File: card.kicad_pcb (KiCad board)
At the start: 2 copper layers, 55 x 85 mm, 9 parts, among them CON1 USB-MINI-B, IC1 ATTINY44-S, P1 CONN_3X2

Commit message: rev C to fab
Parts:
- P1: moved to B.Cu
- moved D1 0.98 mm to (189.5, 88.5), turned to 270 degrees
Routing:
- net +5V: track 32.5 -> 43.7 mm, vias 1 -> 2
- net /MOSI: track 48.8 -> 59.4 mm, vias 1 -> 2
- net (no net): track 265.4 -> 257.0 mm
- net /SCK: track 37.0 -> 29.5 mm, vias 0 -> 2
- net /RST: track 30.9 -> 24.7 mm, vias 1 -> 2
- net GND: track 48.6 -> 52.4 mm, vias 3 -> 4
- net /MISO: track 32.0 -> 28.5 mm
- net N-0000017: track 11.3 -> 12.4 mm
- net N-0000016: track 13.7 -> 12.9 mm
- added copper zone on B.Cu, net (none)
- removed copper zone on F.Cu, net GND
- removed copper zone on B.Cu, net N-000001
- removed copper zone on B.Cu, net N-000002
- removed copper zone on B.Cu, net N-000003
- removed copper zone on B.Cu, net N-000005
- removed copper zone on B.Cu, net N-000006
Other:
- outline, holes or cut-outs redrawn
- board text removed: "CUTOUT"

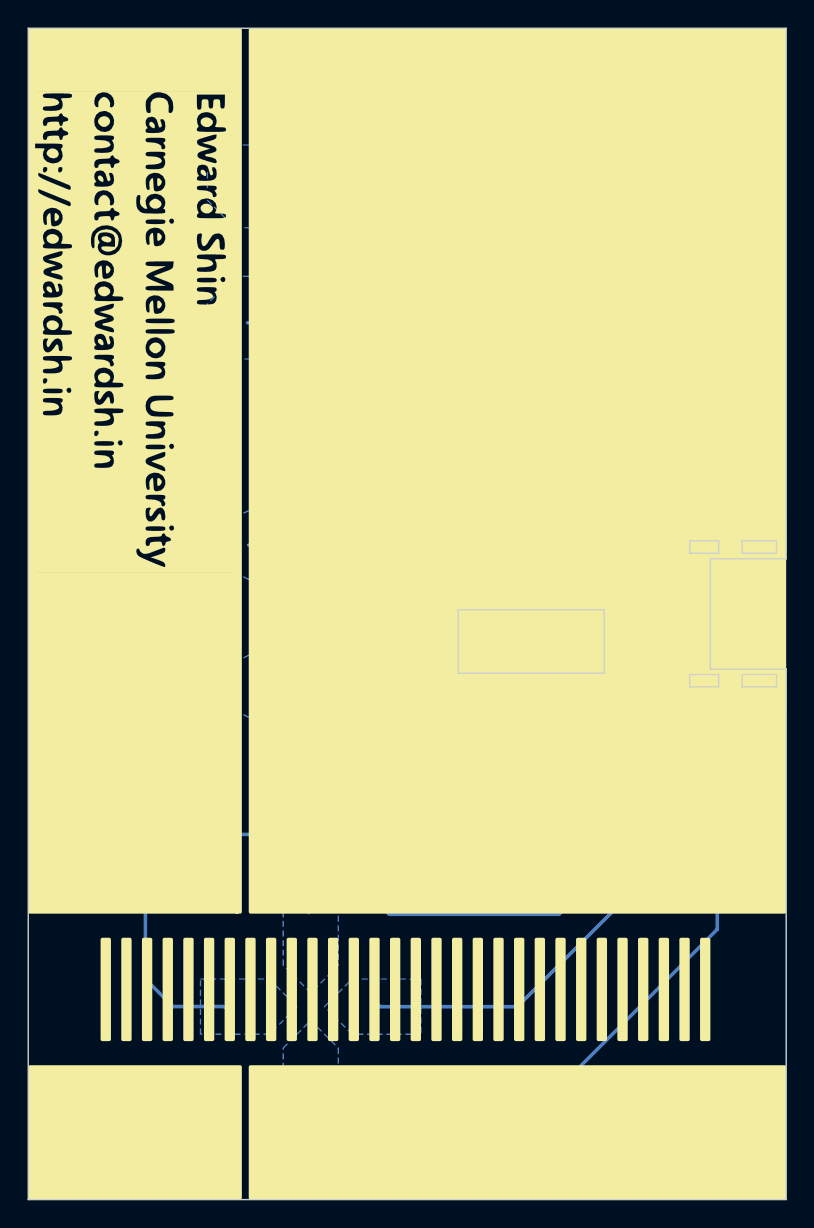
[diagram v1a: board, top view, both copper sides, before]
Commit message: working attiny26 rev sent to oshpark
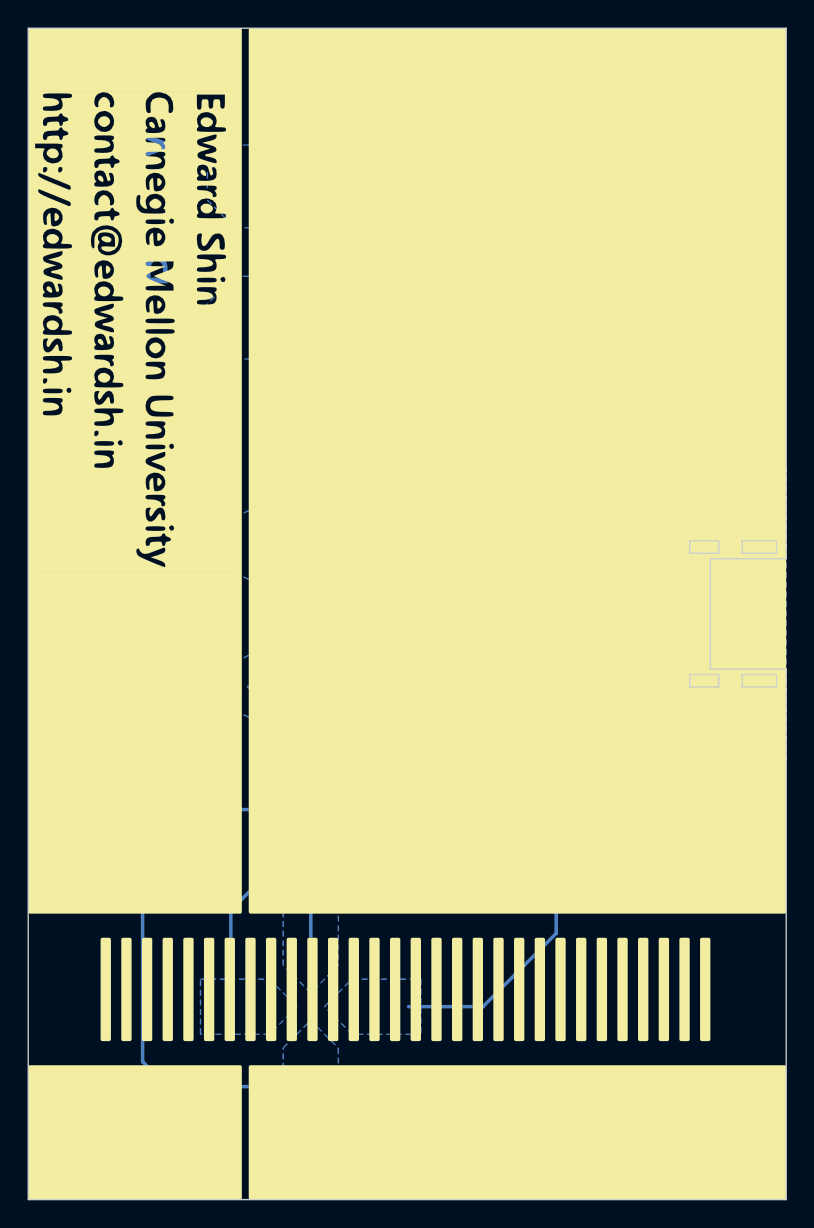
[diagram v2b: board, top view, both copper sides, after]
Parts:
- added R2: 4.7k, Resistors_SMD:R_0603_HandSoldering, B.Cu at (186.3, 85.4)
- C1: footprint SM0402_c -> Capacitors_SMD:C_0603_HandSoldering
- CON1: footprint 15542661MicroUSBB -> card:15542661MicroUSBB
- D1: footprint SMini4-F3-B -> card:SMini4-F3-B
- IC1: value ATTINY44-S -> ATTINY26-S; footprint so-14-inverted -> Housings_SOIC:SOIC-20_7.5x12.8mm_Pitch1.27mm
- P1: footprint pin_array_3x2_no_silk -> Pin_Headers:Pin_Header_Straight_2x03
- R1: footprint SM0603 -> Resistors_SMD:R_0603_HandSoldering
- RP1: footprint MNR12 -> card:MNR12
- moved P1 25.8 mm to (175.6, 80.8), turned to 270 degrees
- moved IC1 4.38 mm to (177.6, 92.5), turned to 270 degrees
- moved RP1 2.50 mm to (186.4, 89.2)
- moved C1 2.21 mm to (187.3, 97.6)
- moved R1 1.30 mm to (187.3, 93.1)
- moved D1 0.69 mm to (189.6, 89.2)
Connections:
- CON1 pad 4: (no net) -> Net-(CON1-Pad4)
- IC1 pad 1: +5V -> /MOSI
- IC1 pad 10: (no net) -> /RST
- IC1 pad 11: (no net) -> /Up
- IC1 pad 12: (no net) -> /Right
- IC1 pad 13: (no net) -> /Down
- IC1 pad 14: GND -> /Left
- IC1 pad 2: (no net) -> /MISO
- IC1 pad 3: N-000009 -> /SCK
- IC1 pad 4: /RST -> Net-(IC1-Pad4)
- IC1 pad 5: N-0000013 -> +5V
- IC1 pad 6: (no net) -> GND
- IC1 pad 7: /MOSI -> /Start
- IC1 pad 8: /MISO -> Net-(IC1-Pad8)
- IC1 pad 9: /SCK -> Net-(IC1-Pad9)
- RP1 pad 1: N-000009 -> Net-(IC1-Pad8)
- RP1 pad 2: N-0000013 -> Net-(IC1-Pad9)
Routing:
- net (no net): track 257.0 -> 0.00 mm
- net /Left: track 0.00 -> 59.4 mm
- net /MOSI: track 59.4 -> 12.0 mm, vias 2 -> 1
- net /A: track 0.00 -> 42.0 mm
- net /Down: track 0.00 -> 37.5 mm
- net /Up: track 0.00 -> 31.4 mm
- net /B: track 0.00 -> 31.2 mm
- net /Right: track 0.00 -> 29.3 mm
- net +5V: track 43.7 -> 70.1 mm, vias 2 -> 4
- net /Start: track 0.00 -> 22.3 mm, vias 0 -> 2
- net /MISO: track 28.5 -> 11.2 mm
- net /Select: track 0.00 -> 16.7 mm
- net /RST: track 24.7 -> 11.7 mm, vias 2 -> 0
- net /SCK: track 29.5 -> 16.8 mm, vias 2 -> 1
- net Net-(IC1-Pad8): track 0.00 -> 8.31 mm
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- added copper zone on B.Cu, net /A
- added copper zone on B.Cu, net /B
- added copper zone on B.Cu, net /Down
- added copper zone on B.Cu, net /Left
- added copper zone on B.Cu, net /Right
- added copper zone on B.Cu, net /Select
- added copper zone on B.Cu, net /Start
- added copper zone on B.Cu, net /Up
- removed copper zone on B.Cu, net (none)
- removed copper zone on B.Cu, net /MISO
- removed copper zone on B.Cu, net /MOSI
- removed copper zone on B.Cu, net /SCK
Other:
- outline, holes or cut-outs redrawn

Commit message: v3, updated with exposed capacitive pads
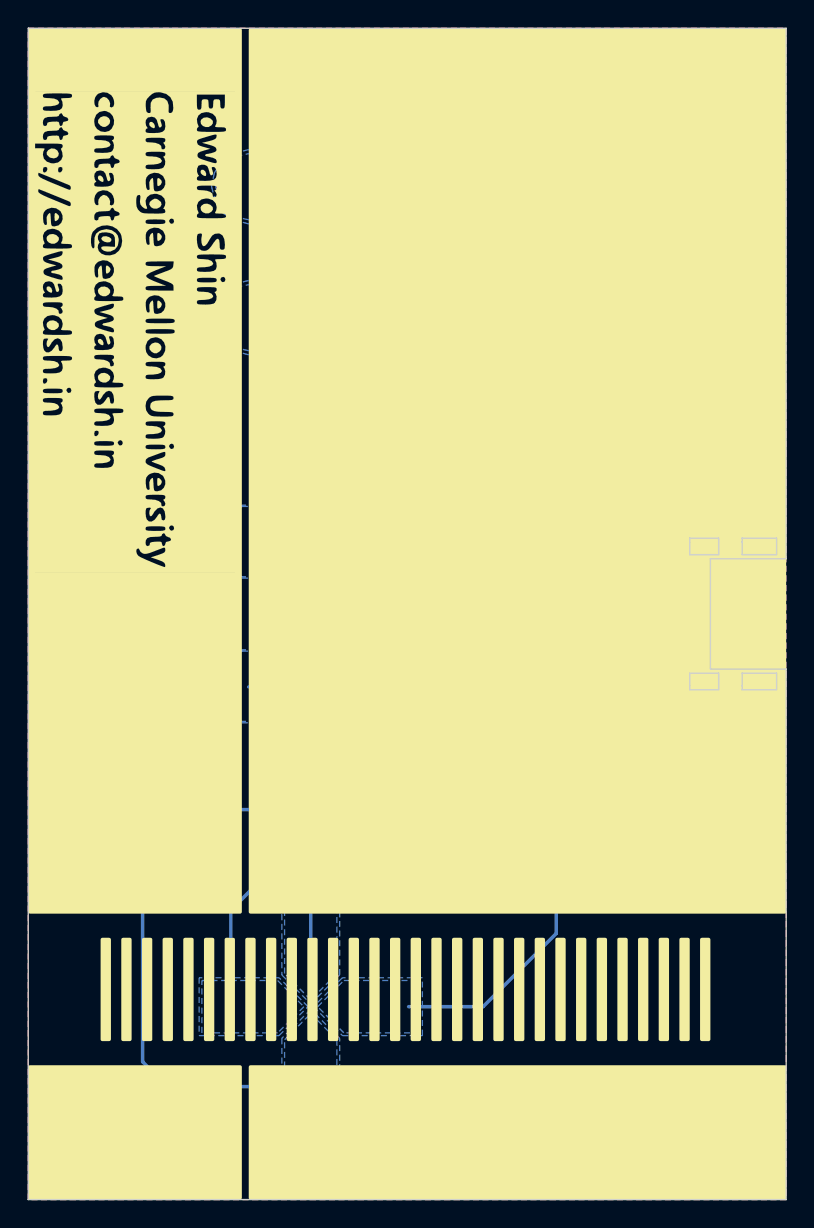
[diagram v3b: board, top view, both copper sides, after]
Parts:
- moved P1 1.90 mm to (175.6, 82.7)
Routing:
- net /SCK: track 16.8 -> 12.8 mm
- net /MISO: track 11.2 -> 7.68 mm
- net /RST: track 11.7 -> 9.83 mm
- net +5V: track 70.1 -> 68.2 mm
- net /Start: track 22.3 -> 23.3 mm
- net /MOSI: track 12.0 -> 11.5 mm
- added copper zone on F.Cu, net GND
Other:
- outline, holes or cut-outs redrawn
